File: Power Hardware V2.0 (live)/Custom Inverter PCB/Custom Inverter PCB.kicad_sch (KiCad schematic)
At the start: 0 parts

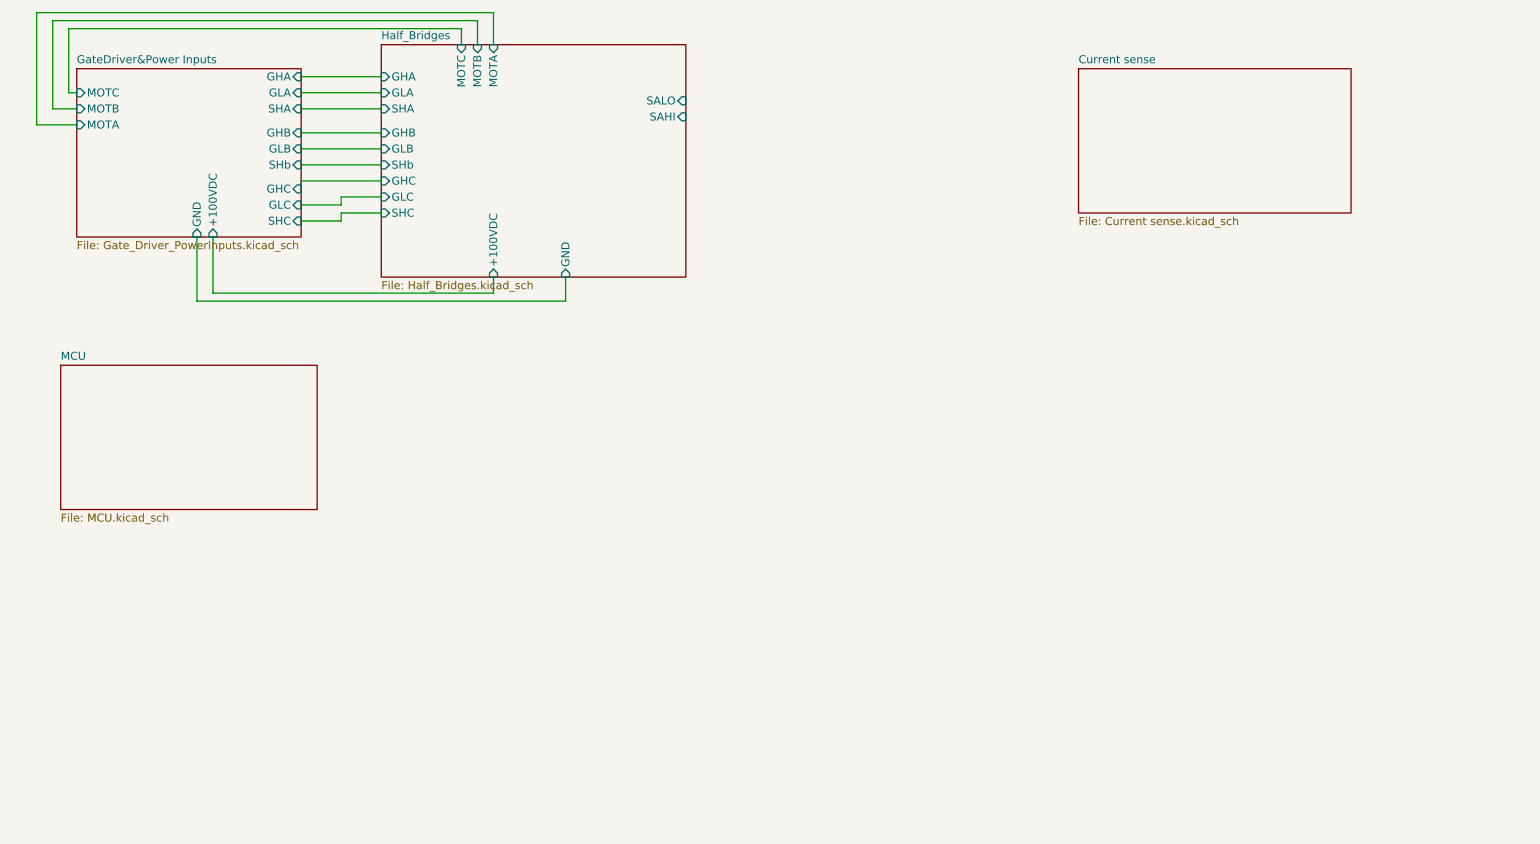
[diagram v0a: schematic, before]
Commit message: switches instead of relays. Short on half bridge fixed. encoder page made. root page connections fixed
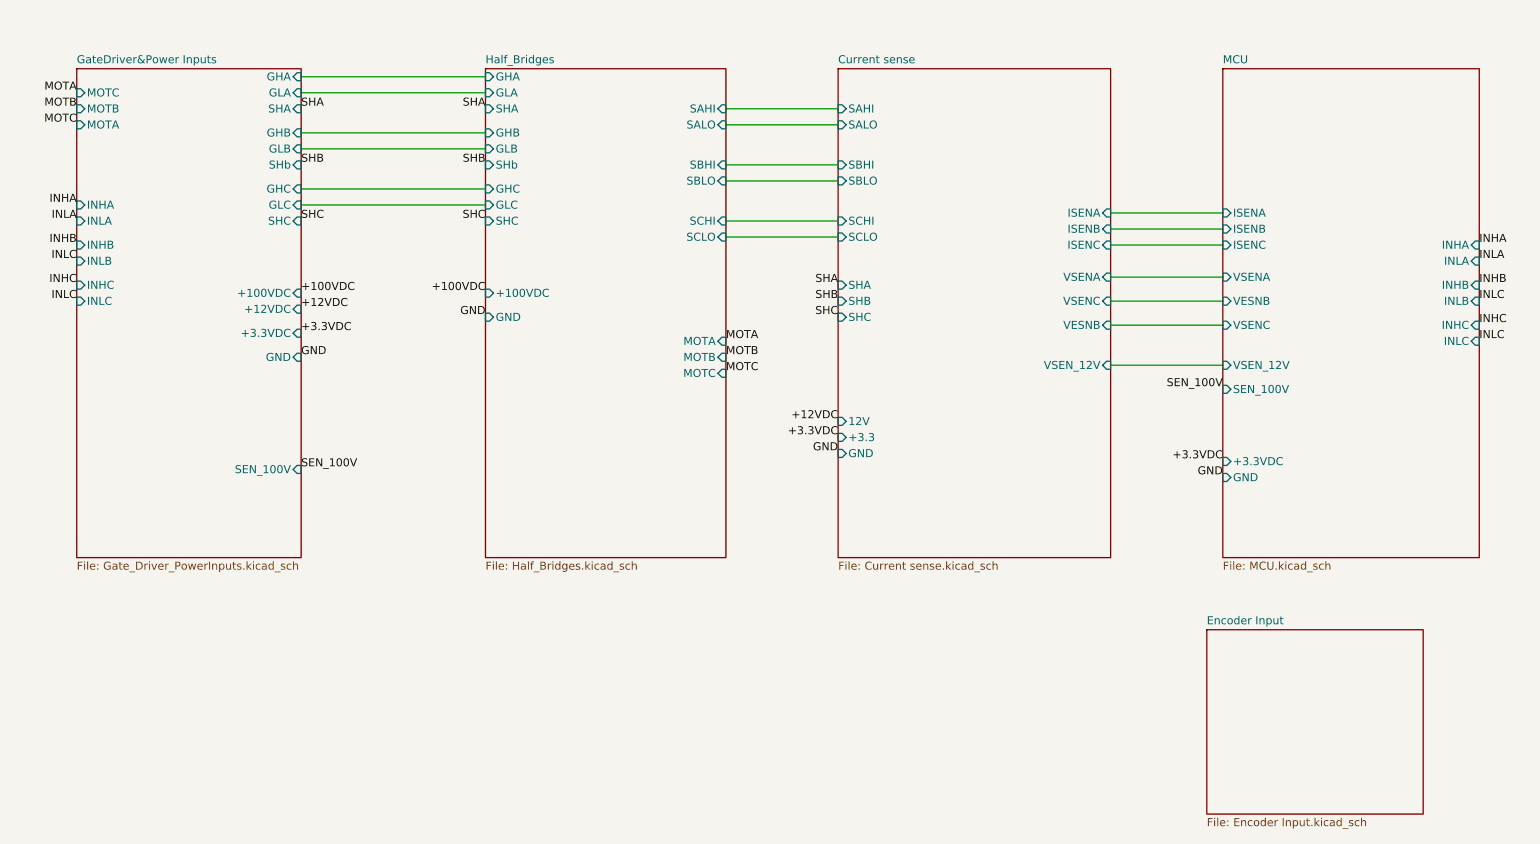
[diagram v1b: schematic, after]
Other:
- added sheet Encoder Input (Encoder Input.kicad_sch)
- sheet Current sense ports: added +3.3, 12V, GND, ISENA, ISENB, ISENC, SAHI, SALO, SBHI, SBLO, SCHI, SCLO, SHA, SHB, SHC, VESNB, VSENA, VSENC, VSEN_12V; removed none
- sheet GateDriver&Power Inputs ports: added +12VDC, +3.3VDC, INHA, INHB, INHC, INLA, INLB, INLC, SEN_100V; removed none
- sheet Half_Bridges ports: added SBHI, SBLO, SCHI, SCLO; removed none
- sheet MCU ports: added +3.3VDC, GND, INHA, INHB, INHC, INLA, INLB, INLC, ISENA, ISENB, ISENC, SEN_100V, VESNB, VSENA, VSENC, VSEN_12V; removed none

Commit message: Schematic Changes
-Changed 3.3V regulator to a higher power unit for the sin-cos circuit (from 500mA to 3A)
-Fixed flipped MOTA,B,C connection to Output Terminal
- Current Sense IC setup
- Fuses for Phase current outputs
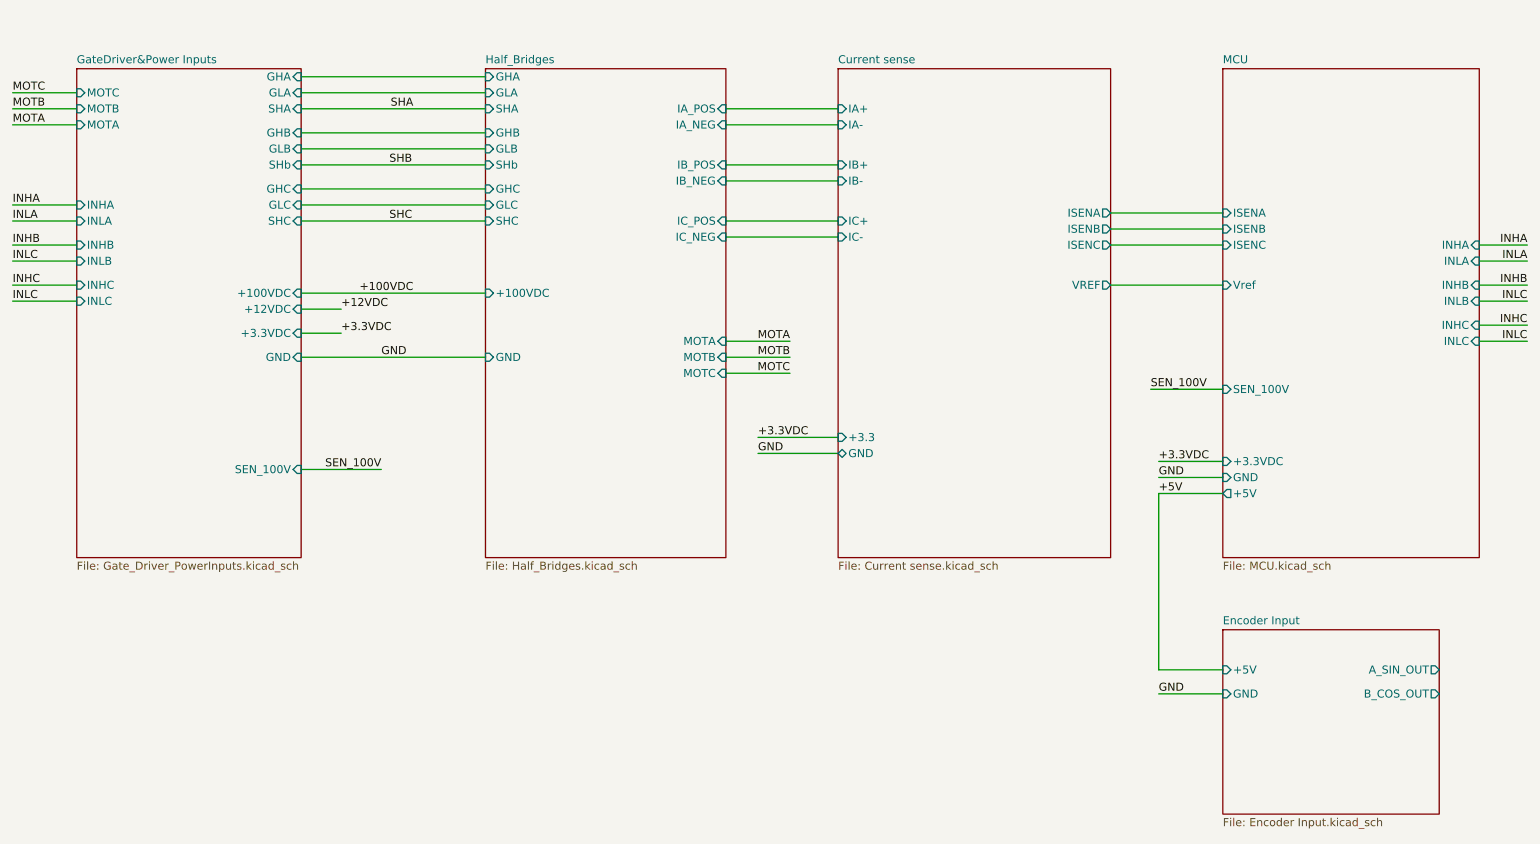
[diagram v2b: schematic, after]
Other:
- sheet Current sense ports: added IA+, IA-, IB+, IB-, IC+, IC-, VREF; removed 12V, SAHI, SALO, SBHI, SBLO, SCHI, SCLO, SHA, SHB, SHC, VESNB, VSENA, VSENC, VSEN_12V
- sheet Encoder Input ports: added +5V, A_SIN_OUT, B_COS_OUT, GND; removed none
- sheet Half_Bridges ports: added IA_NEG, IA_POS, IB_NEG, IB_POS, IC_NEG, IC_POS; removed SAHI, SALO, SBHI, SBLO, SCHI, SCLO
- sheet MCU ports: added +5V, Vref; removed VESNB, VSENA, VSENC, VSEN_12V

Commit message: Pcb layout and tracing
changed footprint file for current sense ic
did layout and tracing for pcb
created bom
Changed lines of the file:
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@@
 		)
 	)
-	(label "INLC"
+	(label "INLB"
 		(at 264.16 62.23 180)
 		(effects
@@
 		)
 	)
-	(label "INLC"
+	(label "INLB"
 		(at 24.13 55.88 0)
 		(effects
